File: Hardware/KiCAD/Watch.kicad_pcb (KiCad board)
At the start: 2 copper layers, 32 x 32 mm, 39 parts, among them IC101 PT7C4563BQ1WEX, IC201 IS31FL3235A-QFLS2-TR, U101 ATSAM4LS2AA-AU, U102 MCP73831-2-OT, Y101 CM8V-T1A-32.768kHz-4pF-20PPM-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

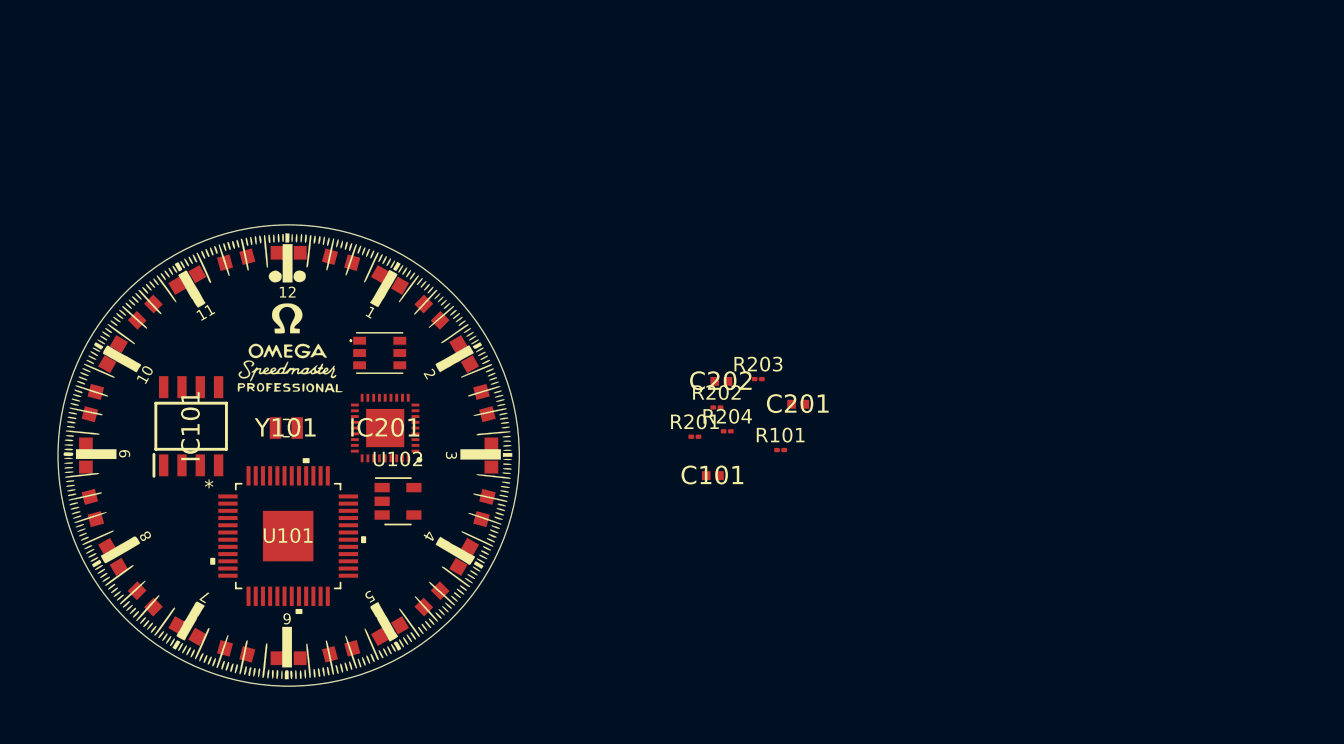
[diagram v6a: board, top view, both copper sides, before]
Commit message: Added various necessary circuits such as light sensor, button pads, RTC cleanup.
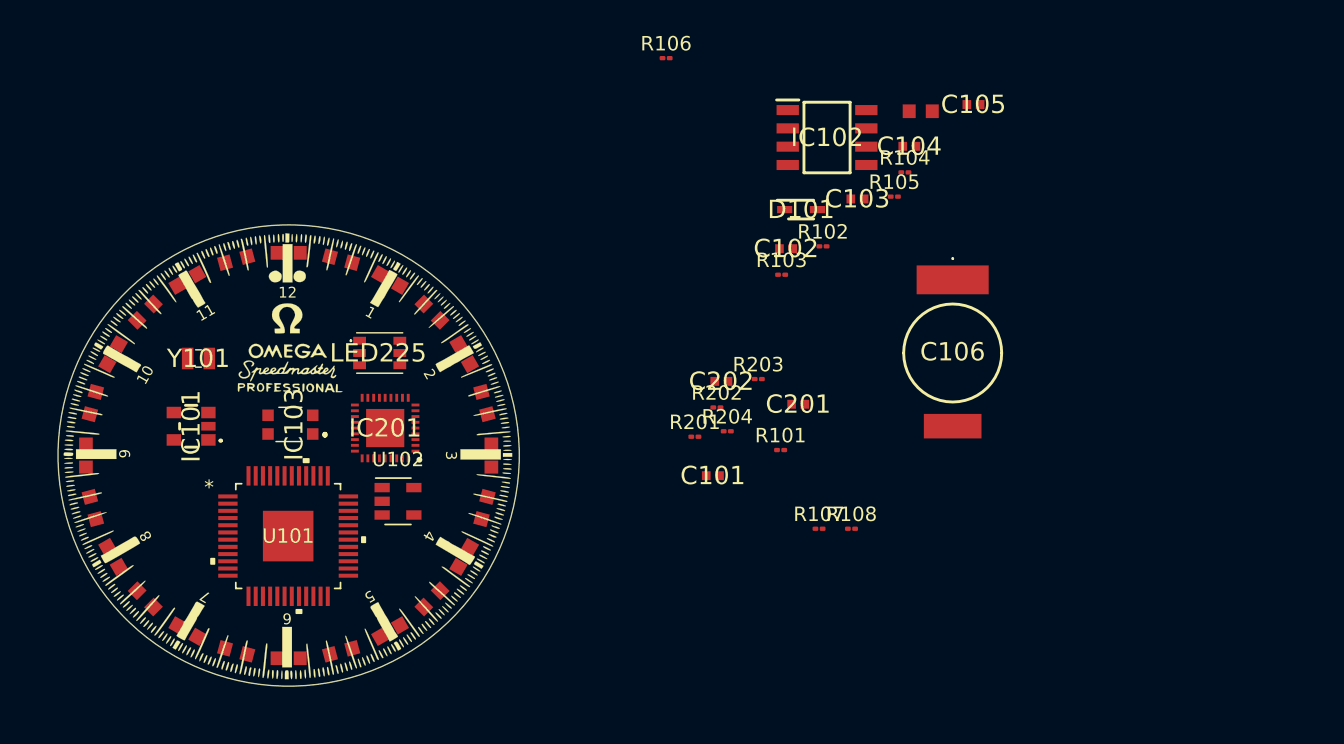
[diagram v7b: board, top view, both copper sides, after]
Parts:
- added C102: 4.7uF, SamacSys_Parts:CAPC1005X55N, F.Cu at (180.3, 73.9)
- added C103: 0.1uF, SamacSys_Parts:CAPC1005X55N, F.Cu at (185.3, 70.5)
- added C104: 0.1uF, SamacSys_Parts:CAPC1005X55N, F.Cu at (188.9, 66.8)
- added C105: 0.1uF, SamacSys_Parts:CAPC1005X55N, F.Cu at (193.3, 63.9)
- added C106: RSCSK2043R3D01004T, SamacSys_Parts:RSCSK2043R3D01004T, F.Cu at (191.9, 81.2)
- added D101: CUS520,H3F, SamacSys_Parts:SOD2513X115N, F.Cu at (181.4, 71.2)
- added IC102: PCF85063AT_AY, SamacSys_Parts:SOIC127P600X175-8N, F.Cu at (183.2, 66.2)
- added IC103: SFH_5711-2_3-Z, SamacSys_Parts:SFH571123Z, F.Cu at (145.9, 86.1)
- added LED101: LTST-C191KRKT, SamacSys_Parts:LEDC1608X55N, F.Cu at (189.7, 64.4)
- added R102: 470, Resistor_SMD:R_01005_0402Metric, F.Cu at (182.9, 73.8)
- added R103: 4.7k, Resistor_SMD:R_01005_0402Metric, F.Cu at (180.0, 75.7)
- added R104: 4.7k, Resistor_SMD:R_01005_0402Metric, F.Cu at (188.6, 68.6)
- added R105: 4.7k, Resistor_SMD:R_01005_0402Metric, F.Cu at (187.8, 70.3)
- added R106: 56k, Resistor_SMD:R_01005_0402Metric, F.Cu at (172.0, 60.7)
- added R107: 10k, Resistor_SMD:R_01005_0402Metric, F.Cu at (182.6, 93.3)
- added R108: 10k, Resistor_SMD:R_01005_0402Metric, F.Cu at (184.9, 93.3)
- C101: value ?uF -> 4.7uF
- IC101: value PT7C4563BQ1WEX -> TCR2LF33,LM_CT; footprint SamacSys_Parts:SOIC127P600X175-8N -> SamacSys_Parts:TCR2LF33LMCT
- moved Y101 7.78 mm to (139.6, 81.5)
- renumbered LED206 to LED201, LED206 to LED202, LED206 to LED203, LED206 to LED204, LED206 to LED205, LED206 to LED207, LED206 to LED208, LED206 to LED209, LED206 to LED210, LED206 to LED211, LED206 to LED212, LED206 to LED213, LED206 to LED214, LED206 to LED215, LED206 to LED216, LED206 to LED217, LED206 to LED218, LED206 to LED219, LED206 to LED220, LED206 to LED221, LED206 to LED222, LED206 to LED223, LED206 to LED224
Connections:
- net Net-(U101-Pad7) renamed +1V8
- C101 pad 1: Net-(C101-Pad1) -> GND
- C101 pad 2: Net-(C101-Pad2) -> +5V
- C201 pad 1: +3V3 -> Net-(C201-Pad1)
- C201 pad 2: GND -> Net-(C201-Pad2)
- IC101 pad 1: Net-(C101-Pad2) -> +BATT
- IC101 pad 2: Net-(IC101-Pad2) -> GND
- IC101 pad 3: Net-(IC101-Pad3) -> +BATT
- IC101 pad 4: GND -> Net-(IC101-Pad4)
- IC101 pad 5: /SDA -> +3V3
- LED201 pad 1: /leds/OUT6 -> /leds/OUT1
- LED202 pad 1: /leds/OUT6 -> /leds/OUT2
- LED203 pad 1: /leds/OUT6 -> /leds/OUT3
- LED204 pad 1: /leds/OUT6 -> /leds/OUT4
- LED205 pad 1: /leds/OUT6 -> /leds/OUT5
- LED207 pad 1: /leds/OUT6 -> /leds/OUT7
- LED208 pad 1: /leds/OUT6 -> /leds/OUT8
- LED209 pad 1: /leds/OUT6 -> /leds/OUT9
- LED210 pad 1: /leds/OUT6 -> /leds/OUT10
- LED211 pad 1: /leds/OUT6 -> /leds/OUT12
- LED212 pad 1: /leds/OUT6 -> /leds/OUT13
- LED213 pad 1: /leds/OUT6 -> /leds/OUT14
- LED214 pad 1: /leds/OUT6 -> /leds/OUT15
- LED215 pad 1: /leds/OUT6 -> /leds/OUT16
- LED216 pad 1: /leds/OUT6 -> /leds/OUT17
- LED217 pad 1: /leds/OUT6 -> /leds/OUT18
- LED218 pad 1: /leds/OUT6 -> /leds/OUT19
- LED219 pad 1: /leds/OUT6 -> /leds/OUT20
- LED220 pad 1: /leds/OUT6 -> /leds/OUT21
- LED221 pad 1: /leds/OUT6 -> /leds/OUT21
- LED222 pad 1: /leds/OUT6 -> /leds/OUT22
- LED223 pad 1: /leds/OUT6 -> /leds/OUT23
- LED224 pad 1: /leds/OUT6 -> /leds/OUT24
- U101 pad 17: Net-(U101-Pad17) -> GND
- U101 pad 18: Net-(U101-Pad18) -> +3V3
- U101 pad 19: Net-(U101-Pad19) -> +3V3
- U101 pad 28: Net-(U101-Pad28) -> GND
- U101 pad 29: Net-(U101-Pad29) -> +3V3
- U101 pad 40: Net-(U101-Pad40) -> +3V3
- U101 pad 45: Net-(U101-Pad45) -> +3V3
- U101 pad 48: Net-(U101-Pad48) -> GND
- U101 pad 6: Net-(U101-Pad6) -> GND
- U101 pad 8: Net-(U101-Pad8) -> +3V3
- U102 pad 3: Net-(U102-Pad3) -> +BATT
- Y101 pad 1: Net-(IC101-Pad2) -> Net-(IC102-Pad2)
- Y101 pad 2: Net-(C101-Pad2) -> Net-(IC102-Pad1)

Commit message: First Schematic layout complete
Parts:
- added C107: 0.1uF, SamacSys_Parts:CAPC1005X55N, F.Cu at (199.5, 97.9)
- added C108: 0.1uF, SamacSys_Parts:CAPC1005X55N, F.Cu at (194.3, 99.2)
- added J101: Conn_01x02, Connector_PinHeader_1.27mm:PinHeader_1x02_P1.27mm_Vertical, F.Cu at (200.4, 92.1)
- added J102: Conn_01x01, Connector_PinHeader_1.27mm:PinHeader_1x01_P1.27mm_Vertical, F.Cu at (207.4, 83.7)
- added J103: Conn_01x01, Connector_PinHeader_1.27mm:PinHeader_1x01_P1.27mm_Vertical, F.Cu at (207.4, 87.0)
- added J104: Conn_ARM_JTAG_SWD_10, Connector_PinHeader_1.27mm:PinHeader_2x05_P1.27mm_Vertical_SMD, F.Cu at (193.3, 94.0)
- added J105: Conn_01x02, Connector_PinHeader_1.27mm:PinHeader_1x02_P1.27mm_Vertical, F.Cu at (205.1, 92.1)
- added LED102: LTST-C191KRKT, SamacSys_Parts:LEDC1608X55N, F.Cu at (190.7, 99.6)
- added R109: 10k, Resistor_SMD:R_01005_0402Metric, F.Cu at (202.1, 97.8)
- added R110: 10k, Resistor_SMD:R_01005_0402Metric, F.Cu at (196.9, 99.0)
- added R111: 10k, Resistor_SMD:R_01005_0402Metric, F.Cu at (199.1, 99.7)
- added R112: 10k, Resistor_SMD:R_01005_0402Metric, F.Cu at (202.1, 99.4)
- added R113: 1Meg, Resistor_SMD:R_01005_0402Metric, F.Cu at (204.3, 97.8)
- added R114: 1MEG, Resistor_SMD:R_01005_0402Metric, F.Cu at (204.3, 99.4)
- added TP101: TestPoint, TestPoint:TestPoint_Pad_D1.0mm, F.Cu at (211.2, 83.8)
- added TP102: TestPoint, TestPoint:TestPoint_Pad_D1.0mm, F.Cu at (211.3, 87.5)
- added TP103: TestPoint, TestPoint:TestPoint_Pad_D1.0mm, F.Cu at (211.3, 90.6)
- added TP104: TestPoint, TestPoint:TestPoint_Pad_D1.0mm, F.Cu at (214.4, 87.5)
- added TP105: TestPoint, TestPoint:TestPoint_Pad_D1.0mm, F.Cu at (214.4, 90.6)
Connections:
- IC201 pad 29: /leds/SDB -> /SDB
- R204 pad 1: /leds/SDB -> /SDB
- U101 pad 1: Net-(U101-Pad1) -> /SW1
- U101 pad 10: Net-(U101-Pad10) -> /JTAG_TMS
- U101 pad 11: Net-(U101-Pad11) -> /vLUX
- U101 pad 12: Net-(U101-Pad12) -> /BattSns
- U101 pad 2: Net-(U101-Pad2) -> /SW2
- U101 pad 3: Net-(U101-Pad3) -> /LED_STAT
- U101 pad 39: Net-(U101-Pad39) -> /SDB
- U101 pad 4: Net-(U101-Pad4) -> /JTAG_RESET
- U101 pad 41: Net-(U101-Pad41) -> /SDA
- U101 pad 42: Net-(U101-Pad42) -> /SCL
- U101 pad 43: Net-(U101-Pad43) -> /JTAG_TDO
- U101 pad 44: Net-(U101-Pad44) -> /JTAG_TDI
- U101 pad 9: Net-(U101-Pad9) -> /JTAG_TCK
- U101 pad EPAD: Net-(U101-PadEPAD) -> GND
